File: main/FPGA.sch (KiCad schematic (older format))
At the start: 44 parts, among them IC4 ESP-PSRAM64H, J8 FPGA_debug, J9 FPGA_GPIO, U3 XC7A100T-FTG256, U4 S25FL127S, X1 20MHz Oscillator

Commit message: Fix up after review
Done:
- Add bulk decoupling capacitor to switch regulator cirucit
- Disconnect DONE from PROGRAM_B in FPGA (mistake)
- The decoupling capacitors used for the FPGA were for the 15T, not the
  100T. It was also setup for two I/O banks, we only use one. Disconnect
  I/O bank 15.
- Switch external clock on the MCU to an oscillator, allowing for 72MHz
- Switch pinout of the backup SPI on the MCU so that half the pins are
  ground

Mizzing:
- Add low-pass filters to the output of the DAC as per the datasheet.
  May remove the need for the amplifier circuit.
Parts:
- removed C48: 47uF, symbol Device:C
- removed C49, C50: 4.7uF, symbol Device:C
- removed C51, C52, C55: 470nF, symbol Device:C
- added C32, C33, C34, C35: 4.7uF, Resistor_SMD:R_0805_2012Metric_Pad1.20x1.40mm_HandSolder, symbol Device:C
- added C38, C39, C40, C41, C42, C43, C61, C62: 470nF, Resistor_SMD:R_0603_1608Metric_Pad0.98x0.95mm_HandSolder, symbol Device:C
- C29: renamed from C28; value 100uF -> 330uF
- C30: renamed from C32; footprint (none) -> Resistor_SMD:R_0805_2012Metric_Pad1.20x1.40mm_HandSolder
- C31: renamed from C36; footprint (none) -> Resistor_SMD:R_0805_2012Metric_Pad1.20x1.40mm_HandSolder
- C36: renamed from C39; footprint (none) -> Resistor_SMD:R_0603_1608Metric_Pad0.98x0.95mm_HandSolder
- C37: renamed from C42; footprint (none) -> Resistor_SMD:R_0603_1608Metric_Pad0.98x0.95mm_HandSolder
- C45: renamed from C29; footprint (none) -> Resistor_SMD:R_1210_3225Metric_Pad1.30x2.65mm_HandSolder
- C46: renamed from C33; footprint (none) -> Resistor_SMD:R_0805_2012Metric_Pad1.20x1.40mm_HandSolder
- C47: renamed from C37; footprint (none) -> Resistor_SMD:R_0805_2012Metric_Pad1.20x1.40mm_HandSolder
- C48: renamed from C40; footprint (none) -> Resistor_SMD:R_0603_1608Metric_Pad0.98x0.95mm_HandSolder
- C49: renamed from C43; footprint (none) -> Resistor_SMD:R_0603_1608Metric_Pad0.98x0.95mm_HandSolder
- C50: renamed from C45; footprint (none) -> Resistor_SMD:R_0603_1608Metric_Pad0.98x0.95mm_HandSolder
- C51: renamed from C30; value 47uF -> 100uF; footprint (none) -> Resistor_SMD:R_1210_3225Metric_Pad1.30x2.65mm_HandSolder
- C52: renamed from C34; footprint (none) -> Resistor_SMD:R_0603_1608Metric_Pad0.98x0.95mm_HandSolder
- C53: footprint (none) -> Resistor_SMD:R_0603_1608Metric_Pad0.98x0.95mm_HandSolder
- C54: renamed from C31; footprint (none) -> Resistor_SMD:R_1210_3225Metric_Pad1.30x2.65mm_HandSolder
- C55: renamed from C35; footprint (none) -> Resistor_SMD:R_1210_3225Metric_Pad1.30x2.65mm_HandSolder
- C56: renamed from C38; footprint (none) -> Resistor_SMD:R_0805_2012Metric_Pad1.20x1.40mm_HandSolder
- C57: renamed from C41; footprint (none) -> Resistor_SMD:R_0805_2012Metric_Pad1.20x1.40mm_HandSolder
- C58: renamed from C44; footprint (none) -> Resistor_SMD:R_0603_1608Metric_Pad0.98x0.95mm_HandSolder
- C59: renamed from C46; footprint (none) -> Resistor_SMD:R_0603_1608Metric_Pad0.98x0.95mm_HandSolder
- C60: renamed from C47; footprint (none) -> Resistor_SMD:R_0603_1608Metric_Pad0.98x0.95mm_HandSolder
- C63: renamed from C56; footprint (none) -> Resistor_SMD:R_0603_1608Metric_Pad0.98x0.95mm_HandSolder
- IC4: footprint SOIC127P600X175-8N -> ESP-PSRAM64H:SOIC127P600X175-8N
- R32: footprint (none) -> Resistor_SMD:R_0805_2012Metric_Pad1.20x1.40mm_HandSolder
- R33: renamed from R35; footprint (none) -> Resistor_SMD:R_0805_2012Metric_Pad1.20x1.40mm_HandSolder
- R34: renamed from R39; footprint (none) -> Resistor_SMD:R_0805_2012Metric_Pad1.20x1.40mm_HandSolder
- R35: renamed from R33; footprint (none) -> Resistor_SMD:R_0805_2012Metric_Pad1.20x1.40mm_HandSolder
- R36: renamed from R34; footprint (none) -> Resistor_SMD:R_0805_2012Metric_Pad1.20x1.40mm_HandSolder
- R37: renamed from R36; footprint (none) -> Resistor_SMD:R_0805_2012Metric_Pad1.20x1.40mm_HandSolder
- R38: renamed from R37; footprint (none) -> Resistor_SMD:R_0805_2012Metric_Pad1.20x1.40mm_HandSolder
- R39: renamed from R38; footprint (none) -> Resistor_SMD:R_0805_2012Metric_Pad1.20x1.40mm_HandSolder
- X1: value 20MHz Oscillator -> FGPA Oscillator (20MHZ)
- renumbered C27 to C28, C54 to C44, U4 to U3, U3 to U4
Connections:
- net +1V0: now also C53.1, C32.1, C33.1, C34.1, C35.1, C38.1, C39.1, C40.1, C41.1, C42.1, C43.1
- net +3V3: now also C61.1, C62.1; no longer C53.1, U4.A16 (VCCO_15), U4.B13 (VCCO_15), U4.C10 (VCCO_15), U4.E14 (VCCO_15), U4.H15 (VCCO_15), U4.J12 (VCCO_15)
- net GND: now also C32.2, C33.2, C34.2, C35.2, C38.2, C39.2, C40.2, C41.2, C42.2, C43.2, C61.2, C62.2
- net MCU_clock_in renamed MCU_CLOCK_IN
- net done renamed PROGRAM_B
- net PROGRAM_B: no longer U4.H10 (DONE_0)
- new net DONE: U4.H10 (DONE_0)
- no-connect marks 69 -> 75
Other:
- note added: "1 x 100uF, 2 x 470nF\n"
- note added: "1 x 330uF, 6 x 4.7uF, 8 x 470nF"
- note added: "1 x 47uF, 2 x 4.7uF, 3 x 470nF"
- note added: "One I/O Bank (14): 1 x 47uF or 100uF, 2 x 4.7 uF, 4 x 470nF"
- moved on the sheet: C29, C30, C31, C36, C37, C45, C46, C47, C48, C49, C50, C51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

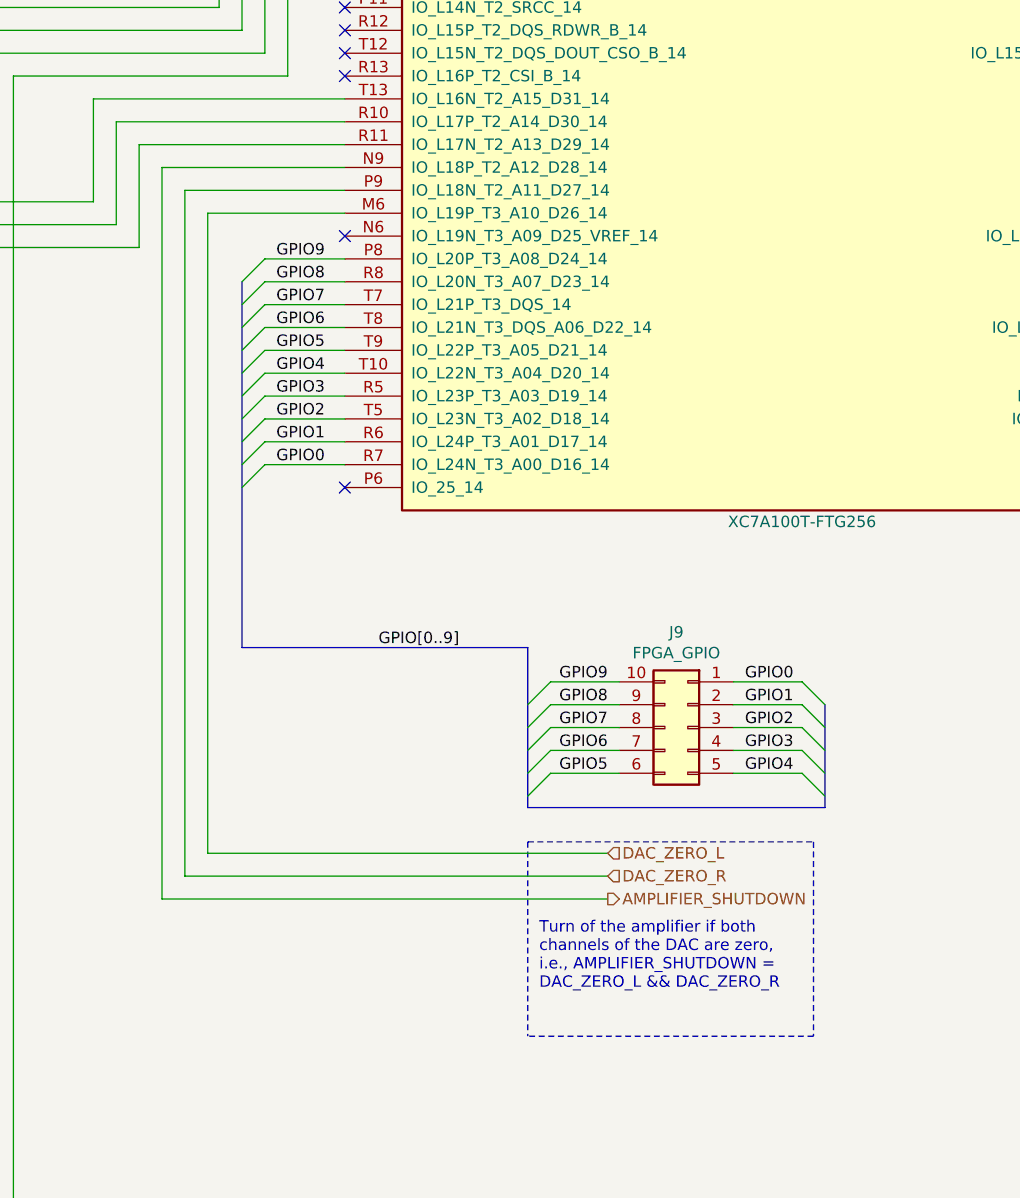
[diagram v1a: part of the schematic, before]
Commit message: Fix up after review 2
Don't route DAC_ZERO_{L,R} through FPGA into SHUTDOWN on the amp, it is
not really necessary and just adds routing complexity.
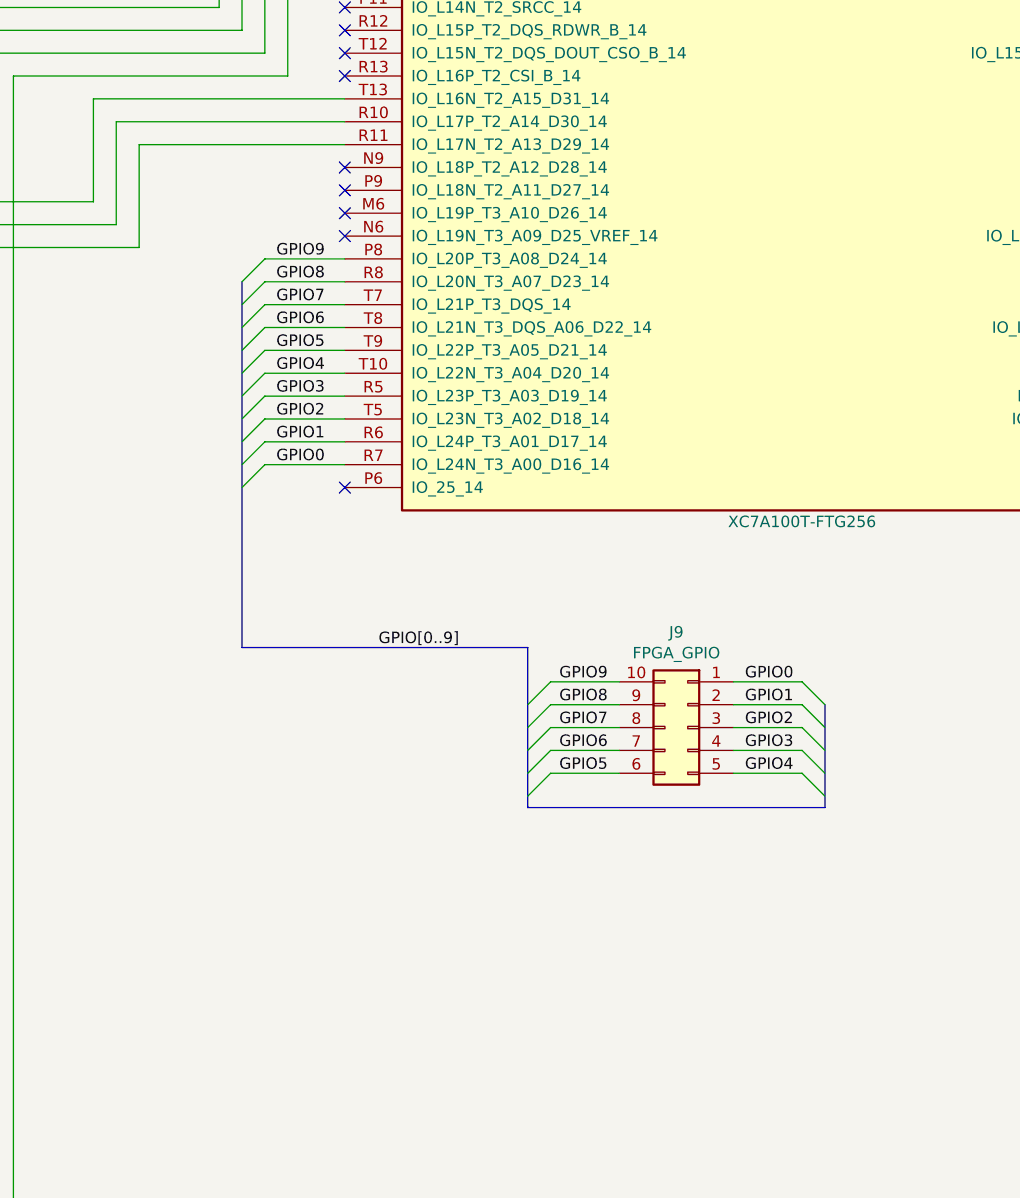
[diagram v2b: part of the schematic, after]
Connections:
- net AMPLIFIER_SHUTDOWN: no longer names the net of U4.N9 (IO_L18P_T2_A12_D28_14)
- net DAC_ZERO_L: no longer names the net of U4.M6 (IO_L19P_T3_A10_D26_14)
- net DAC_ZERO_R: no longer names the net of U4.P9 (IO_L18N_T2_A11_D27_14)
- no-connect marks 75 -> 78
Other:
- note removed: "Turn of the amplifier if both\nchannels of the DAC are zero,\ni.e., AMPLIFIER_SHUTDOWN = \nDAC_ZERO_L && DAC_ZERO_R"
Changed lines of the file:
@@
 Text HLabel 9800 3450 0    50   Output ~ 0
 DAC_SYS_CLK
-Text HLabel 13050 8250 2    50   Input ~ 0
-DAC_ZERO_L
-Text HLabel 13050 8350 2    50   Input ~ 0
-DAC_ZERO_R
-Text HLabel 13050 8450 2    50   Output ~ 0
-AMPLIFIER_SHUTDOWN
-Wire Wire Line
-	11100 8450 13050 8450
 Wire Wire Line
 	10400 3350 10400 3450
 Wire Wire Line
 	10400 3450 9800 3450
-Text Notes 12750 8850 0    50   ~ 0
-Turn of the amplifier if both\nchannels of the DAC are zero,\ni.e., AMPLIFIER_SHUTDOWN = \nDAC_ZERO_L && DAC_ZERO_R
-Wire Notes Line
-	12700 8200 13950 8200
-Wire Notes Line
-	13950 8200 13950 9050
-Wire Notes Line
-	13950 9050 12700 9050
-Wire Notes Line
-	12700 8200 12700 9050
 Wire Wire Line
 	11550 6550 11900 6550
@@
 Wire Wire Line
 	9700 5600 11000 5600
-Wire Wire Line
-	11300 8250 11300 5450
-Wire Wire Line
-	11300 5450 11900 5450
-Wire Wire Line
-	11300 8250 13050 8250
-Wire Wire Line
-	11200 8350 11200 5350
-Wire Wire Line
-	11200 5350 11900 5350
-Wire Wire Line
-	11200 8350 13050 8350
-Wire Wire Line
-	11100 8450 11100 5250
-Wire Wire Line
-	11100 5250 11900 5250
 Wire Wire Line
 	9550 10400 9550 10050
@@
 Text Notes 3800 9800 0    50   ~ 0
 One I/O Bank (14): 1 x 47uF or 100uF, 2 x 4.7 uF, 4 x 470nF
+NoConn ~ 11900 5450
+NoConn ~ 11900 5350
+NoConn ~ 11900 5250
 Wire Bus Line
 	10250 3150 10250 3350

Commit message: Fix up after review 3
Add +3.3V and GND to MCU and FPGA GPIO.

Add a lot of footprints.
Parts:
- removed J9: FPGA_GPIO, symbol Connector_Generic:Conn_02x05_Counter_Clockwise
- added J4: FPGA_GPIO, symbol Connector_Generic:Conn_02x06_Odd_Even
- C30, C31, C32, C33, C34, C35, C46, C47, C56, C57: footprint Resistor_SMD:R_0805_2012Metric_Pad1.20x1.40mm_HandSolder -> Capacitor_SMD:C_0805_2012Metric_Pad1.18x1.45mm_HandSolder
- C36, C37, C38, C39, C40, C41, C42, C43, C48, C49, C50, C52, C53, C58, C59, C60, C61, C62, C63: footprint Resistor_SMD:R_0603_1608Metric_Pad0.98x0.95mm_HandSolder -> Capacitor_SMD:C_0603_1608Metric_Pad1.08x0.95mm_HandSolder
- C45, C51, C54, C55: footprint Resistor_SMD:R_1210_3225Metric_Pad1.30x2.65mm_HandSolder -> Capacitor_SMD:C_1210_3225Metric_Pad1.33x2.70mm_HandSolder
- U4: footprint (none) -> Package_BGA:Xilinx_FTG256
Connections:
- net +3V3: now also J4.11 (Pin_11)
- net GND: now also J4.12 (Pin_12)
- net GPIO0: now also J4.1 (Pin_1)
- net GPIO1: now also J4.3 (Pin_3)
- net GPIO2: now also J4.5 (Pin_5)
- net GPIO3: now also J4.7 (Pin_7)
- net GPIO4: now also J4.9 (Pin_9)
- net GPIO5: now also J4.10 (Pin_10)
- net GPIO6: now also J4.8 (Pin_8)
- net GPIO7: now also J4.6 (Pin_6)
- net GPIO8: now also J4.4 (Pin_4)
- net GPIO9: now also J4.2 (Pin_2)

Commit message: DAC: Remove amplifier, replace with low pass as per datasheet
Also: a lot of footprint association
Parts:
- removed X1: FGPA Oscillator (20MHZ), Oscillator:Oscillator_DIP-8, symbol Oscillator:CXO_DIP8
- added unit 2 of U3
- added X1: FGPA_Oscillator, symbol Oscillator:TXC-7C
- C19: renamed from C28; footprint (none) -> Capacitor_SMD:C_0805_2012Metric_Pad1.18x1.45mm_HandSolder
- C35: renamed from C44; footprint (none) -> Capacitor_SMD:C_0805_2012Metric_Pad1.18x1.45mm_HandSolder
- J4: renamed from J8; footprint (none) -> Connector_PinHeader_2.00mm:PinHeader_2x07_P2.00mm_Vertical
- J5: renamed from J4; footprint (none) -> Connector_PinHeader_2.54mm:PinHeader_2x06_P2.54mm_Vertical
- U2: renamed from U3; footprint (none) -> Package_SO:SOIC-8_5.275x5.275mm_P1.27mm
- renumbered C29 to C20, C30 to C21, C31 to C22, C32 to C23, C33 to C24, C34 to C25, C35 to C26, C36 to C27, C37 to C28, C38 to C29, C39 to C30, C40 to C31, C41 to C32, C42 to C33, C43 to C34, C45 to C36, C46 to C37, C47 to C38, C48 to C39, C49 to C40, C50 to C41, C51 to C42, C52 to C43, C53 to C44, C54 to C45, C55 to C46, C56 to C47, C57 to C48, C58 to C49, C59 to C50, C60 to C51, C61 to C52, C62 to C53, C63 to C54, IC4 to IC3, R32 to R18, R33 to R19, R34 to R20, R35 to R21, R36 to R22, R37 to R23, R38 to R24, R39 to R25, U4 to U3
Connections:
- net +3V3: now also X1.1 (EN), X1.4 (Vdd); no longer IC3.7 (SIO[3]), U3.P13 (IO_L11N_T1_SRCC_14)
- net GND: now also U3.A16 (VCCO_15), U3.B13 (VCCO_15), U3.C10 (VCCO_15), U3.E14 (VCCO_15), U3.H15 (VCCO_15), U3.J12 (VCCO_15), U3.A6 (VCCO_35), U3.B3 (VCCO_35), U3.D7 (VCCO_35), U3.E4 (VCCO_35), U3.F1 (VCCO_35), U3.J2 (VCCO_35), U3.M3 (VCCO_34), U3.R4 (VCCO_34), U3.T1 (VCCO_34), X1.2 (GND)
- net at U3.P14 (IO_L12N_T1_MRCC_14): now also X1.3 (OUT)
- new net: IC3.7 (SIO[3]), U3.P13 (IO_L11N_T1_SRCC_14)
- no-connect marks 78 -> 142

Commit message: Start PCB layout
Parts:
- C20: footprint (none) -> Capacitor_Tantalum_SMD:CP_EIA-7343-43_Kemet-X_Pad2.25x2.55mm_HandSolder
- IC3: Manufacturer_Name Espressif Systems -> Adafruit Industries; Manufacturer_Part_Number ESP-PSRAM64H -> 4677; URL (none) -> https://www.digikey.com/en/products/detail/adafruit-industr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
- J5: Manufacturer_Name (none) -> Multicomp PRO; Manufacturer_Part_Number (none) -> 2213S-50G; URL (none) -> https://no.farnell.com/multicomp/2213s-50g/connector-header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
- U2: Description (none) -> Flash for the FPGA; Manufacturer_Name (none) -> Cypress; Manufacturer_Part_Number (none) -> S25FL127SABMFV101; URL (none) -> https://no.farnell.com/cypress-semiconductor/s25fl127sabmfv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
- U3: Manufacturer_Name (none) -> Xilinx; Manufacturer_Part_Number (none) -> XC7A100T-FTG256
- X1: footprint (none) -> Oscillator:Oscillator_SMD_SeikoEpson_SG210-4Pin_2.5x2.0mm_HandSoldering
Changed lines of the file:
@@
 F 1 "XC7A100T-FTG256" H 1950 10976 50  0000 C CNN
 F 2 "Package_BGA:Xilinx_FTG256" H 1950 9500 50  0001 C CNN
-F 3 "" H 1950 9500 50  0000 C CNN
+F 3 "https://www.google.com/url?sa=t&rct=j&q=&esrc=s&source=web&cd=&cad=rja&uact=8&ved=2ahUKEwiH1rrnlZ_zAhUrtYsKHcsIDFQQFnoECAUQAQ&url=https%3A%2F%2Fwww.xilinx.com%2Fsupport%2Fdocumentation%2Fuser_guides%2Fug475_7Series_Pkg_Pinout.pdf&usg=AOvVaw3NyLHDtSbZv1hXp1wxMn0l" H 1950 9500 50  0000 C CNN
+F 4 "Xilinx" H 1950 9500 50  0001 C CNN "Manufacturer_Name"
+F 5 "XC7A100T-FTG256" H 1950 9500 50  0001 C CNN "Manufacturer_Part_Number"
 	4    1950 9500
 	1    0    0    -1
@@
 F 1 "XC7A100T-FTG256" H 6900 6850 50  0000 R CNN
 F 2 "Package_BGA:Xilinx_FTG256" H 7450 5400 50  0001 C CNN
-F 3 "" H 7450 5400 50  0000 C CNN
+F 3 "https://www.google.com/url?sa=t&rct=j&q=&esrc=s&source=web&cd=&cad=rja&uact=8&ved=2ahUKEwiH1rrnlZ_zAhUrtYsKHcsIDFQQFnoECAUQAQ&url=https%3A%2F%2Fwww.xilinx.com%2Fsupport%2Fdocumentation%2Fuser_guides%2Fug475_7Series_Pkg_Pinout.pdf&usg=AOvVaw3NyLHDtSbZv1hXp1wxMn0l" H 7450 5400 50  0000 C CNN
+F 4 "Xilinx" H 7450 5400 50  0001 C CNN "Manufacturer_Name"
+F 5 "XC7A100T-FTG256" H 7450 5400 50  0001 C CNN "Manufacturer_Part_Number"
 	3    7450 5400
 	-1   0    0    1
@@
 F 0 "C20" H 1400 7600 50  0000 L CNN
 F 1 "330uF" H 1400 7400 50  0000 L CNN
-F 2 "" H 1350 7500 50  0001 C CNN
+F 2 "Capacitor_Tantalum_SMD:CP_EIA-7343-43_Kemet-X_Pad2.25x2.55mm_HandSolder" H 1350 7500 50  0001 C CNN
 F 3 "~" H 1350 7500 50  0001 C CNN
 	1    1350 7500
@@
 F 2 "Package_SO:SOIC-8_5.275x5.275mm_P1.27mm" H 4250 3250 50  0001 C CNN
 F 3 "https://www.farnell.com/datasheets/2330438.pdf" H 4250 3250 50  0001 C CNN
+F 4 "Flash for the FPGA" H 4700 3200 50  0001 C CNN "Description"
+F 5 "Cypress" H 4700 3200 50  0001 C CNN "Manufacturer_Name"
+F 6 "S25FL127SABMFV101" H 4700 3200 50  0001 C CNN "Manufacturer_Part_Number"
+F 7 "https://no.farnell.com/cypress-semiconductor/s25fl127sabmfv101/flash-memory-128mbit-108mhz-soic/dp/2772749?st=s25fl127s" H 4700 3200 50  0001 C CNN "URL"
 	1    4700 3200
 	1    0    0    -1
@@
 F 1 "ESP-PSRAM64H" H 10450 9950 50  0000 C CNN
 F 2 "ESP-PSRAM64H:SOIC127P600X175-8N" H 11100 10500 50  0001 L CNN
-F 3 "https://www.espressif.com/sites/default/files/documentation/esp-psram64_esp-psram64h_datasheet_en.pdf" H 11100 10400 50  0001 L CNN
+F 3 "https://cdn-shop.adafruit.com/product-files/4677/4677_esp-psram64_esp-psram64h_datasheet_en.pdf" H 11100 10400 50  0001 L CNN
 F 4 "ESP-PSRAM64 and ESP-PSRAM64H 64 Mbit serial pseudo SRAM" H 11100 10300 50  0001 L CNN "Description"
 F 5 "1.75" H 11100 10200 50  0001 L CNN "Height"
-F 6 "Espressif Systems" H 11100 10100 50  0001 L CNN "Manufacturer_Name"
-F 7 "ESP-PSRAM64H" H 11100 10000 50  0001 L CNN "Manufacturer_Part_Number"
+F 6 "Adafruit Industries" H 11100 10100 50  0001 L CNN "Manufacturer_Name"
+F 7 "4677" H 11100 10000 50  0001 L CNN "Manufacturer_Part_Number"
 F 8 "" H 11100 9900 50  0001 L CNN "Mouser Part Number"
 F 9 "" H 11100 9800 50  0001 L CNN "Mouser Price/Stock"
 F 10 "" H 11100 9700 50  0001 L CNN "Arrow Part Number"
 F 11 "" H 11100 9600 50  0001 L CNN "Arrow Price/Stock"
+F 12 "https://www.digikey.com/en/products/detail/adafruit-industries-llc/4677/13148775" H 9650 10400 50  0001 C CNN "URL"
 	1    9650 10400
 	1    0    0    -1
@@
 F 1 "XC7A100T-FTG256" H 13900 900 50  0000 C CNN
 F 2 "Package_BGA:Xilinx_FTG256" H 13900 3850 50  0001 C CNN
-F 3 "" H 13900 3850 50  0000 C CNN
+F 3 "https://www.google.com/url?sa=t&rct=j&q=&esrc=s&source=web&cd=&cad=rja&uact=8&ved=2ahUKEwiH1rrnlZ_zAhUrtYsKHcsIDFQQFnoECAUQAQ&url=https%3A%2F%2Fwww.xilinx.com%2Fsupport%2Fdocumentation%2Fuser_guides%2Fug475_7Series_Pkg_Pinout.pdf&usg=AOvVaw3NyLHDtSbZv1hXp1wxMn0l" H 13900 3850 50  0000 C CNN
+F 4 "Xilinx" H 13900 3850 50  0001 C CNN "Manufacturer_Name"
+F 5 "XC7A100T-FTG256" H 13900 3850 50  0001 C CNN "Manufacturer_Part_Number"
 	1    13900 3850
 	1    0    0    -1
@@
 F 1 "FPGA_GPIO" H 13450 8026 50  0000 C CNN
 F 2 "Connector_PinHeader_2.54mm:PinHeader_2x06_P2.54mm_Vertical" H 13400 7700 50  0001 C CNN
-F 3 "~" H 13400 7700 50  0001 C CNN
+F 3 "https://www.farnell.com/datasheets/3029611.pdf" H 13400 7700 50  0001 C CNN
+F 4 "Multicomp PRO" H 13400 7700 50  0001 C CNN "Manufacturer_Name"
+F 5 "2213S-50G" H 13400 7700 50  0001 C CNN "Manufacturer_Part_Number"
+F 6 "https://no.farnell.com/multicomp/2213s-50g/connector-header-50pos-2-54mm/dp/2847228" H 13400 7700 50  0001 C CNN "URL"
 	1    13400 7700
 	-1   0    0    -1
@@
 F 1 "XC7A100T-FTG256" H 18800 734 50  0000 C CNN
 F 2 "Package_BGA:Xilinx_FTG256" H 18800 3800 50  0001 C CNN
-F 3 "" H 18800 3800 50  0000 C CNN
+F 3 "https://www.google.com/url?sa=t&rct=j&q=&esrc=s&source=web&cd=&cad=rja&uact=8&ved=2ahUKEwiH1rrnlZ_zAhUrtYsKHcsIDFQQFnoECAUQAQ&url=https%3A%2F%2Fwww.xilinx.com%2Fsupport%2Fdocumentation%2Fuser_guides%2Fug475_7Series_Pkg_Pinout.pdf&usg=AOvVaw3NyLHDtSbZv1hXp1wxMn0l" H 18800 3800 50  0000 C CNN
+F 4 "Xilinx" H 18800 3800 50  0001 C CNN "Manufacturer_Name"
+F 5 "XC7A100T-FTG256" H 18800 3800 50  0001 C CNN "Manufacturer_Part_Number"
 	2    18800 3800
 	1    0    0    -1
@@
 F 0 "X1" H 8844 7996 50  0000 L CNN
 F 1 "FGPA_Oscillator" H 8844 7905 50  0000 L CNN
-F 2 "" H 9200 7600 50  0001 C CNN
+F 2 "Oscillator:Oscillator_SMD_SeikoEpson_SG210-4Pin_2.5x2.0mm_HandSoldering" H 9200 7600 50  0001 C CNN
 F 3 "http://www.txccorp.com/download/products/osc/7C_o.pdf" H 8400 7950 50  0001 C CNN
+F 4 "" H 8500 7950 50  0001 C CNN "URL"
 	1    8500 7950
 	1    0    0    -1

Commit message: Continue PCB layout
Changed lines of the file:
@@
 F 1 "XC7A100T-FTG256" H 1950 10976 50  0000 C CNN
 F 2 "Package_BGA:Xilinx_FTG256" H 1950 9500 50  0001 C CNN
-F 3 "https://www.google.com/url?sa=t&rct=j&q=&esrc=s&source=web&cd=&cad=rja&uact=8&ved=2ahUKEwiH1rrnlZ_zAhUrtYsKHcsIDFQQFnoECAUQAQ&url=https%3A%2F%2Fwww.xilinx.com%2Fsupport%2Fdocumentation%2Fuser_guides%2Fug475_7Series_Pkg_Pinout.pdf&usg=AOvVaw3NyLHDtSbZv1hXp1wxMn0l" H 1950 9500 50  0000 C CNN
+F 3 "https://www.google.com/url?sa=t&rct=j&q=&esrc=s&source=web&cd=&cad=rja&uact=8&ved=2ahUKEwiH1rrnlZ_zAhUrtYsKHcsIDFQQFnoECAUQAQ&url=https%3A%2F%2Fwww.xilinx.com%2Fsupport%2Fdocumentation%2Fuser_guides%2Fug475_7Series_Pkg_Pinout.pdf&usg=AOvVaw3NyLHDtSbZv1hXp1wxMn0l" H 1950 9500 50  0001 C CNN
 F 4 "Xilinx" H 1950 9500 50  0001 C CNN "Manufacturer_Name"
 F 5 "XC7A100T-FTG256" H 1950 9500 50  0001 C CNN "Manufacturer_Part_Number"
